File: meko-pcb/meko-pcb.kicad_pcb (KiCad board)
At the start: 6 copper layers, 37 x 69 mm, 210 parts, among them IC2 TPS7A2033PDBVR, IC4 TAD5212IRGER, IC5 AS5600-ASOM, J1 USB_C_Receptacle_USB2.0_16P, J3 GDEY0154D67, J4 Conn_ARM_SWD_TagConnect_TC203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, J5 503398-1892, Q1 SS8050, Q2 Si1308EDL, SW1 SW_Push, SW2 SW_Push, SW3 SW_Push, SW4 SW_Push, SW5 SW_Push, SW6 SW_Push, SW7 SW_Push, SW9 SW_Push, U1 nPM1300-QEXX, U2 nRF5340-QKxx, Y1 32MHz, Y2 32.768 kHz

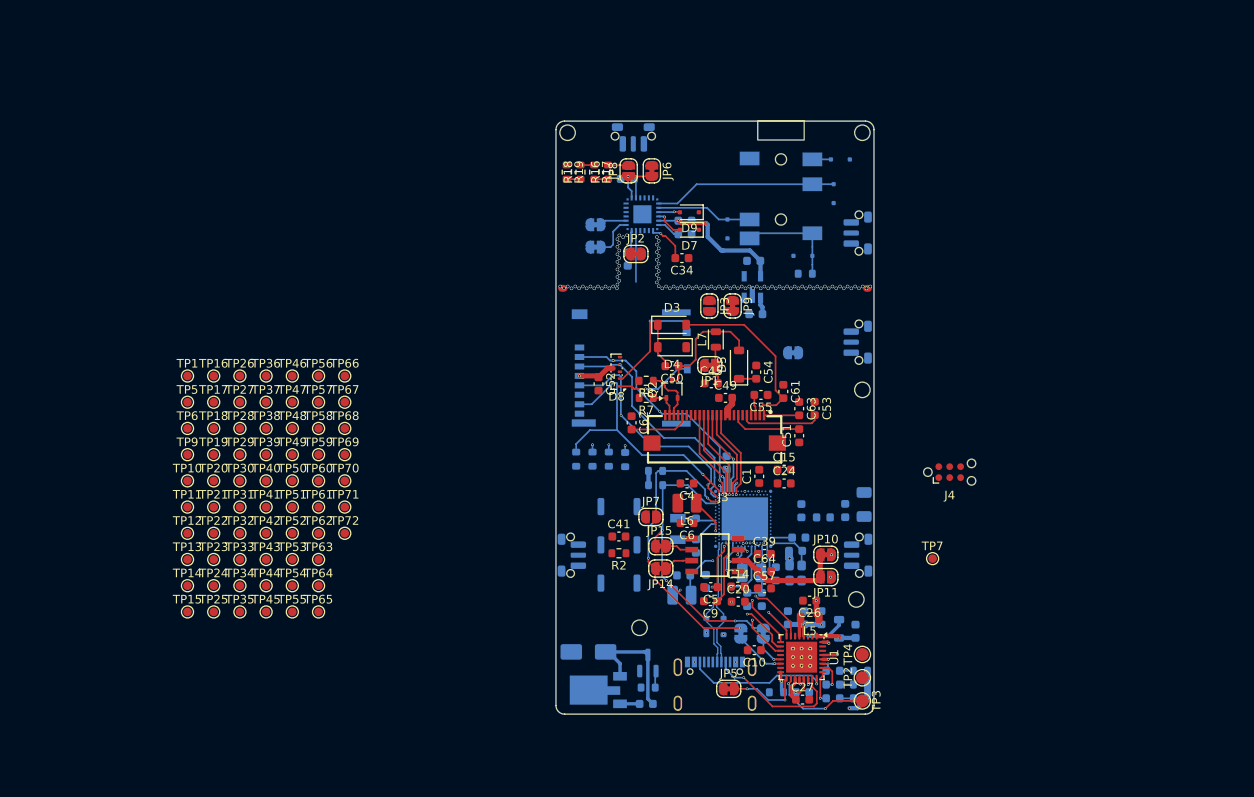
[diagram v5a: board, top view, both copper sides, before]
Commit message: re did the layout of the dac
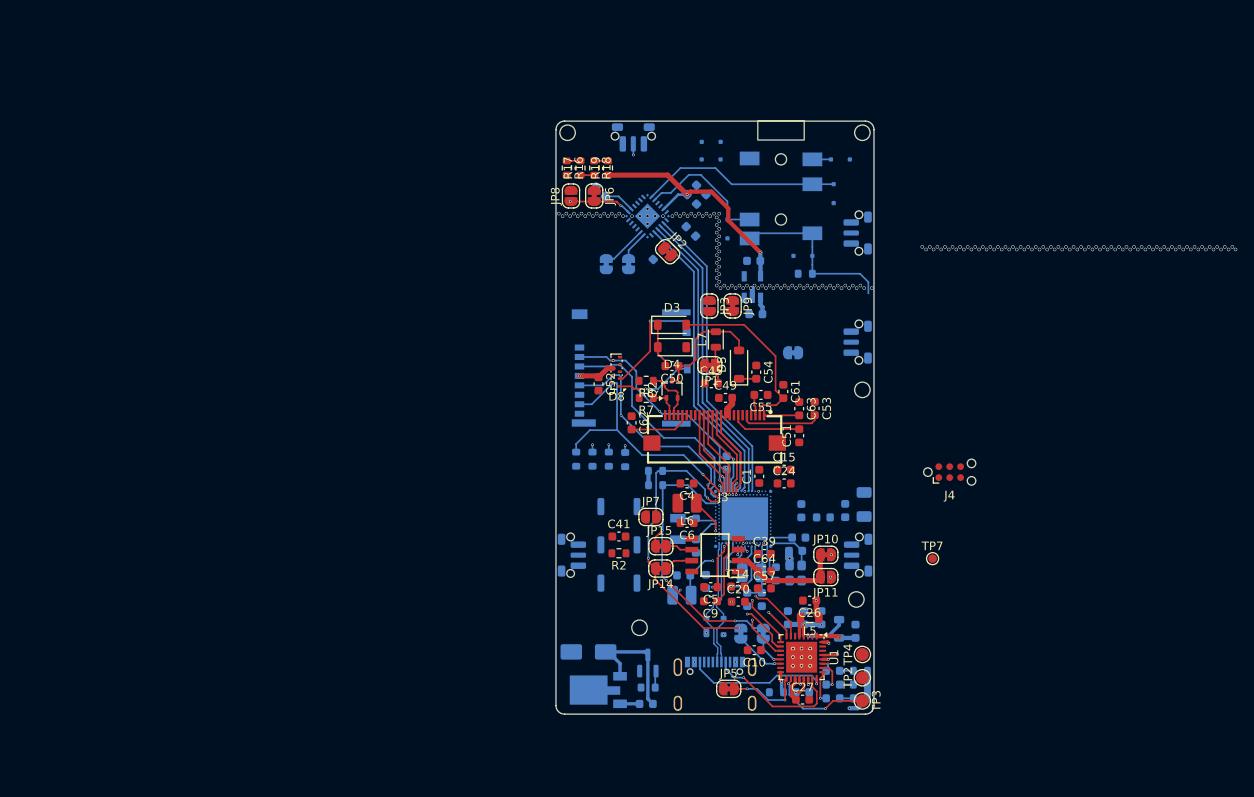
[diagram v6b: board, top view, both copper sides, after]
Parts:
- removed TP1: VOUT1, TestPoint:TestPoint_Pad_D1.0mm
- removed TP10, TP12, TP14, TP16, TP17, TP21, TP22, TP24, TP25, TP27, TP28, TP30, TP31, TP33, TP34, TP36, TP37, TP39, TP40, TP42, TP43, TP44, TP45, TP47, TP48, TP50, TP51, TP53, TP54, TP55, TP56, TP57, TP58, TP59, TP6, TP60, TP61, TP62, TP64, TP66, TP67, TP68, TP69, TP70, TP71, TP72, TP9: DISPL_SDA, TestPoint:TestPoint_Pad_D1.0mm
- removed TP11, TP13, TP15, TP18, TP19, TP20, TP23, TP26, TP29, TP32, TP35, TP38, TP41, TP46, TP49, TP5, TP52, TP63, TP65: DISPL_SCL, TestPoint:TestPoint_Pad_D1.0mm
- C34, D7, D9: moved to B.Cu
- moved D7 10.5 mm to (94.4, 23.4)
- moved JP6 7.31 mm to (80.8, 29.7)
- moved JP8 7.31 mm to (78.0, 29.7)
- moved D9 6.65 mm to (94.3, 25.5)
- moved R16 4.82 mm to (77.5, 26.5), turned to -90 degrees
- moved R19 4.82 mm to (82.3, 26.5), turned to 90 degrees
- moved JP13 4.77 mm to (82.2, 37.7), turned to 90 degrees
- moved C37 4.47 mm to (93.2, 30.1), turned to 45 degrees
- moved JP12 4.34 mm to (84.8, 37.7), turned to 90 degrees
- moved JP2 3.70 mm to (89.3, 36.2), turned to -45 degrees
- moved C30 3.67 mm to (92.1, 29.0), turned to 45 degrees
- moved C44 3.55 mm to (88.2, 36.5), turned to 45 degrees
- moved C42 3.44 mm to (81.5, 29.2), turned to 135 degrees
- moved C34 3.28 mm to (92.0, 33.8), turned to 135 degrees
- moved R17 1.67 mm to (79.2, 26.5), turned to 90 degrees
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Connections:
- U2 pad AK18: /AUDIO_BCLK -> Net-(U2-P0.22)
- U2 pad AK20: /AUDIO_FSYNC -> Net-(U2-P0.23)
- U2 pad AK28: /AUDIO_DIN -> Net-(U2-AIN4/P0.25)
- U2 pad AL13: Net-(U2-P0.19) -> /AUDIO_DIN
- U2 pad AL15: Net-(U2-P0.21) -> /AUDIO_DOUT
- U2 pad AL19: /AUDIO_GPO1 -> /AUDIO_FSYNC
- U2 pad AL21: Net-(U2-P1.06) -> /AUDIO_BCLK
- U2 pad AL23: Net-(U2-P1.08) -> /AUDIO_GPO1
- U2 pad AL27: /AUDIO_DOUT -> Net-(U2-P0.24)
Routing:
- net /BTN_PWR: track 0.00 -> 37.0 mm, vias 0 -> 1
- net /AUDIO_BCLK: track 0.00 -> 35.6 mm
- net /AUDIO_FSYNC: track 0.00 -> 35.1 mm
- net /AUDIO_DOUT: track 0.00 -> 34.9 mm
- net /AUDIO_DIN: track 5.98 -> 34.4 mm
- net +3V3AVDD: track 16.4 -> 28.8 mm
- net /AUDIO_TN: track 12.3 -> 20.5 mm
- net Net-(IC4-DREG): track 4.89 -> 0.00 mm, vias 1 -> 0
- net /OUT_L: track 11.1 -> 15.7 mm
- net Net-(D7-A2): track 3.41 -> 0.00 mm, vias 1 -> 0
- net Net-(IC4-IOVDD): track 2.98 -> 0.00 mm
- net Net-(IC4-VREF): track 2.72 -> 0.00 mm
- net Net-(D9-A2): track 2.50 -> 0.00 mm, vias 1 -> 0
- net Net-(JP8-B): track 2.42 -> 0.04 mm
- net Net-(IC4-SDA): track 3.10 -> 5.26 mm
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
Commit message: moved pin assignments for better layout, redid analog layout
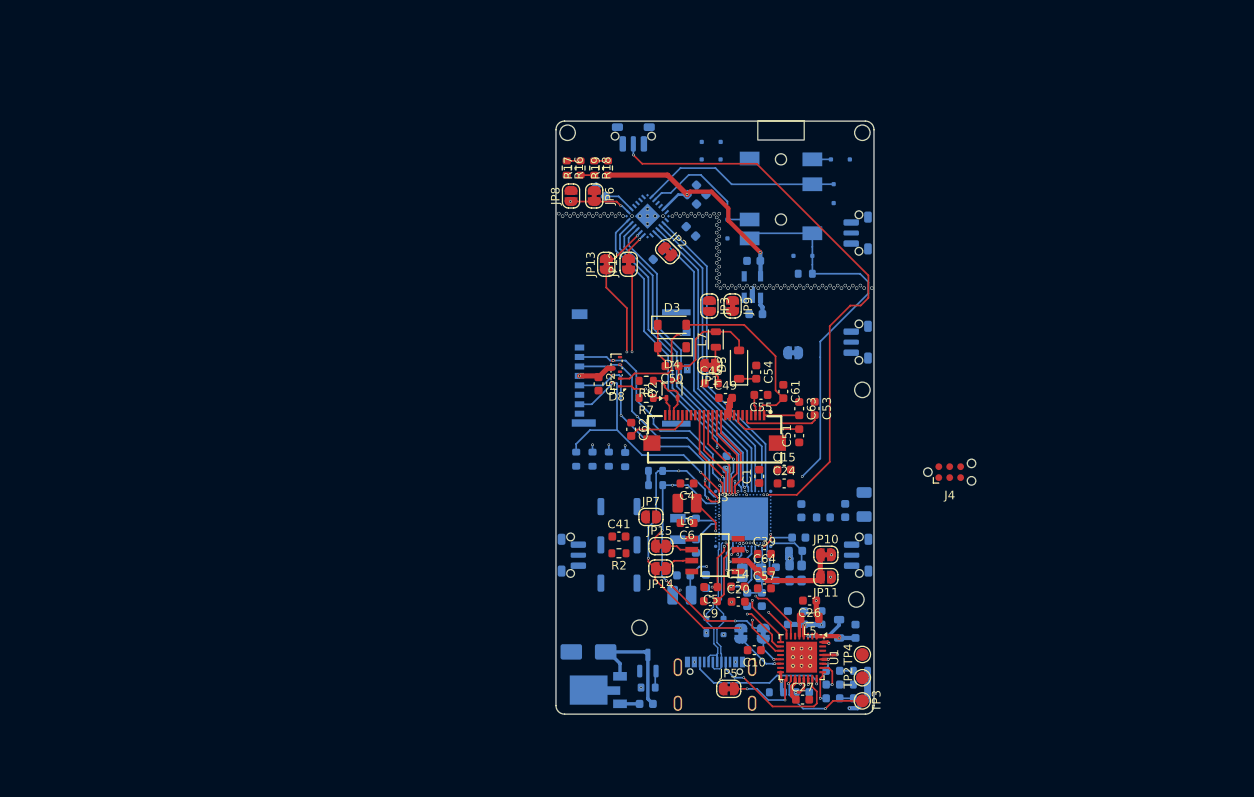
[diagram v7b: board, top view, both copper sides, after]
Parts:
- removed TP7: DISPL_SDA, TestPoint:TestPoint_Pad_D1.0mm
- JP12, JP13: moved to F.Cu
- moved C62 0.75 mm to (85.0, 56.9)
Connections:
- U2 pad AE31: /AUDIO_GPIO1 -> Net-(U2-AIN7/P0.28)
- U2 pad AK14: /BTN_SIDE_R -> /MEM_LEVER
- U2 pad AK16: /BTN_SIDE_L -> Net-(U2-P0.20)
- U2 pad AK18: Net-(U2-P0.22) -> /AUDIO_GPIO2
- U2 pad AK28: Net-(U2-AIN4/P0.25) -> /AUDIO_TN
- U2 pad AK30: /MEM_LEVER -> /BTN_PWR
- U2 pad AL13: /AUDIO_DIN -> /AUDIO_GPI1
- U2 pad AL15: /AUDIO_DOUT -> /AUDIO_GPO1
- U2 pad AL19: /AUDIO_FSYNC -> /AUDIO_GPIO1
- U2 pad AL21: /AUDIO_BCLK -> /AUDIO_DIN
- U2 pad AL23: /AUDIO_GPO1 -> /AUDIO_DOUT
- U2 pad AL27: Net-(U2-P0.24) -> /AUDIO_FSYNC
- U2 pad AL29: /BTN_PWR -> /AUDIO_BCLK
- U2 pad B24: /AUDIO_GPI1 -> /BTN_SIDE_R
- U2 pad R31: /AUDIO_TN -> Net-(U2-P1.10)
- U2 pad U31: /AUDIO_GPIO2 -> Net-(U2-P0.29)
- U2 pad Y2: Net-(U2-AIN1/P0.05) -> /BTN_SIDE_L
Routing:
- net /AUDIO_GPI1: track 0.00 -> 38.1 mm, vias 0 -> 2
- net /AUDIO_GPIO2: track 0.00 -> 38.1 mm, vias 0 -> 2
- net /AUDIO_GPO1: track 0.00 -> 37.6 mm
- net /AUDIO_GPIO1: track 0.00 -> 36.7 mm
- net /AUDIO_TN: track 20.5 -> 51.4 mm, vias 0 -> 2
- net /BTN_PWR: track 37.0 -> 67.6 mm, vias 1 -> 2
- net /I2C_SDA: track 34.1 -> 63.2 mm, vias 3 -> 5
- net /I2C_SCL: track 34.7 -> 61.4 mm, vias 4 -> 6
- net /HAPTIC_MOTOR: track 0.00 -> 23.7 mm, vias 0 -> 2
- net /HAL_OUT: track 0.00 -> 8.57 mm, vias 0 -> 2
- net /D+: track 15.0 -> 17.5 mm
- net /D-: track 15.0 -> 17.4 mm
- net Net-(U2-DECR): track 7.00 -> 8.98 mm, vias 0 -> 2
- net /MEM_LEVER: track 13.8 -> 12.0 mm
- net /MEM_MOSI: track 33.2 -> 32.3 mm
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
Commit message: rf, routed stuff
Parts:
- C41, R2: moved to B.Cu
- moved SW7 28.7 mm to (99.8, 46.6), turned to 0 degrees
- moved R2 27.1 mm to (101.0, 50.6), turned to 0 degrees
- moved C41 26.7 mm to (101.0, 49.1), turned to 180 degrees
- moved J4 25.4 mm to (105.3, 42.8)
- moved R11 10.4 mm to (103.8, 49.1), turned to -90 degrees
- moved JP4 6.92 mm to (100.1, 53.7)
- moved AE1 4.36 mm to (111.0, 61.4), turned to 180 degrees
- moved C13 3.35 mm to (106.6, 66.1), turned to -90 degrees
- moved L1 2.47 mm to (105.2, 66.1), turned to 90 degrees
- moved D9 2.23 mm to (94.1, 23.2)
- moved D7 1.96 mm to (94.1, 25.4)
- moved C18 1.18 mm to (103.7, 66.1)
- moved SW1 0.05 mm to (83.6, 65.9), turned to 0 degrees
- moved SW9 0.05 mm to (83.6, 74.8), turned to 0 degrees
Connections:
- net Net-(AE1-PCB_Trace) renamed /ANTMATCH
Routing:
- net +3V3: track 34.2 -> 228.2 mm, vias 10 -> 33
- net GND: track 2.86 -> 179.5 mm, vias 99 -> 208
- net REG-OUT: track 29.3 -> 118.4 mm, vias 4 -> 5
- net /BTN_VOL_UP: track 0.00 -> 49.6 mm, vias 0 -> 2
- net Net-(U1-SHPHLD): track 0.00 -> 29.9 mm, vias 0 -> 1
- net /SWDCLK: track 0.00 -> 28.4 mm, vias 0 -> 3
- net /SWDIO: track 0.00 -> 27.4 mm, vias 0 -> 3
- net /RESET: track 0.00 -> 25.9 mm, vias 0 -> 3
- net /BTN_SIDE_L: track 0.00 -> 18.8 mm, vias 0 -> 3
- net /PMIC_GPIO0: track 13.4 -> 29.8 mm, vias 2 -> 3
- net /BTN_SIDE_R: track 0.00 -> 13.6 mm, vias 0 -> 3
- net Net-(D9-A2): track 0.00 -> 9.31 mm, vias 0 -> 2
- net /ANTMATCH: track 0.00 -> 7.48 mm
- net Net-(D7-A2): track 0.00 -> 7.47 mm, vias 0 -> 2
- net /ANT: track 0.00 -> 4.70 mm
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- added copper zone on B.Cu, net GND
- added copper zone on F.Cu, net GND
- added copper zone on In2.Cu, net GND
